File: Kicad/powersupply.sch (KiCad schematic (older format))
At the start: 43 parts, among them J901 Jack-DC, J902 Double-mini-DIN-6, J903 Conn_01x05, J904 Header, J905 Header, J906 Conn_01x06, Q901 BC548, SW901 SW_DIP_x01, SW902 SW_DIP_x01, U901 5V DC-DC Module, U902 MAX1615, U903 STM32F031K6T6, U904 TLV1117 3.3V 1A

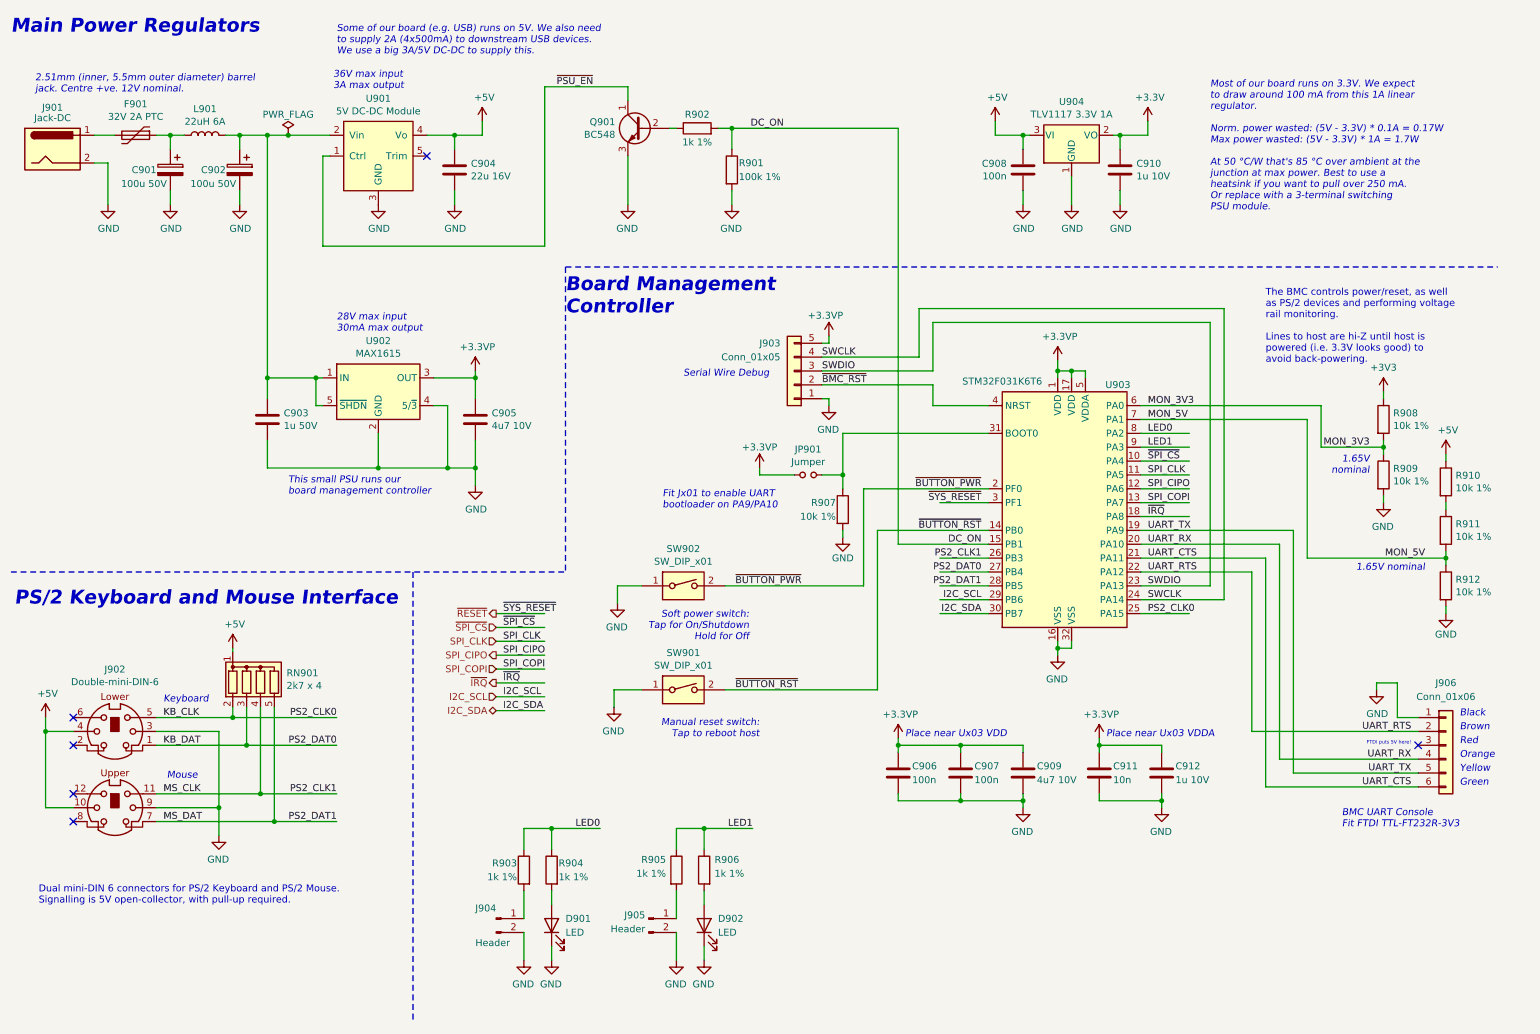
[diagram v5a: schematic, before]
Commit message: Changes to BMC
* Swapped BUTTON_PWR and SYS_RESET to avoid DRC issue
* Split PSU and BMC into two separate sheets
* Swapped some pins on the STM32 to make it compatible with more
alternatives
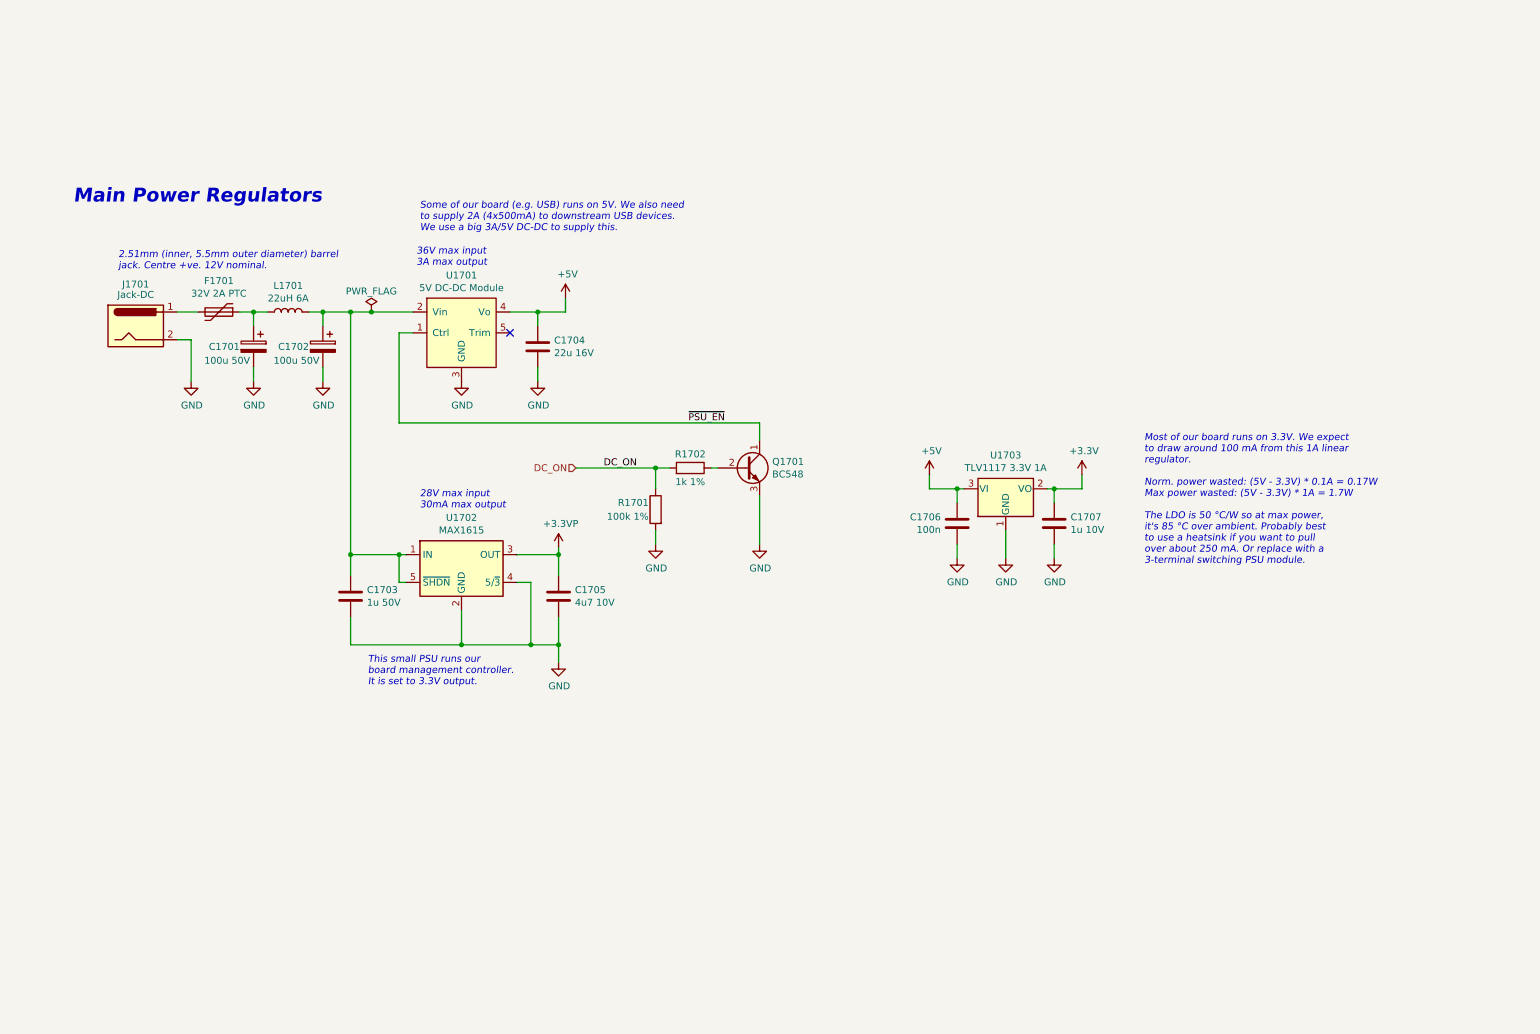
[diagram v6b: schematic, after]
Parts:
- removed C904: 22u 16V, Capacitor_SMD:C_0805_2012Metric_Pad1.18x1.45mm_HandSolder, symbol Device:C
- removed C906, C907, C908: 100n, Capacitor_SMD:C_0805_2012Metric_Pad1.18x1.45mm_HandSolder, symbol Device:C
- removed C909: 4u7 10V, Capacitor_SMD:C_0805_2012Metric_Pad1.18x1.45mm_HandSolder, symbol Device:C
- removed C910, C912: 1u 10V, Capacitor_SMD:C_0805_2012Metric_Pad1.18x1.45mm_HandSolder, symbol Device:C
- removed C911: 10n, Capacitor_SMD:C_0805_2012Metric_Pad1.18x1.45mm_HandSolder, symbol Device:C
- removed D901, D902: LED, LED_THT:LED_D3.0mm, symbol Device:LED
- removed F901: 32V 2A PTC, Fuse:Fuse_BelFuse_0ZRE0016FF_L9.9mm_W3.8mm, symbol Device:Polyfuse
- removed J901: Jack-DC, Connector_BarrelJack:BarrelJack_CUI_PJ-063AH_Horizontal, symbol Connector:Jack-DC
- removed J902: Double-mini-DIN-6, Neotron-Common-Hardware:Double_mini-DIN_6, symbol Neotron-Common-Hardware:Double-mini-DIN-6
- removed J903: Conn_01x05, Connector_PinHeader_2.54mm:PinHeader_1x05_P2.54mm_Vertical, symbol Connector_Generic:Conn_01x05
- removed J904, J905: Header, Connector_PinHeader_2.54mm:PinHeader_1x02_P2.54mm_Vertical, symbol Connector:Conn_01x02_Male
- removed J906: Conn_01x06, Connector_PinHeader_2.54mm:PinHeader_1x06_P2.54mm_Vertical, symbol Connector_Generic:Conn_01x06
- removed JP901: Jumper, Connector_PinHeader_2.54mm:PinHeader_1x02_P2.54mm_Vertical, symbol Device:Jumper_NO_Small
- removed L901: 22uH 6A, Inductor_THT:L_Axial_L26.7mm_D12.1mm_P35.00mm_Horizontal_Vishay_IHA-103, symbol Device:L
- removed R901: 100k 1%, Resistor_SMD:R_0805_2012Metric_Pad1.20x1.40mm_HandSolder, symbol Device:R
- removed R903, R904, R905, R906: 1k 1%, Resistor_SMD:R_0805_2012Metric_Pad1.20x1.40mm_HandSolder, symbol Device:R
- removed R907, R908, R909, R910, R911, R912: 10k 1%, Resistor_SMD:R_0805_2012Metric_Pad1.20x1.40mm_HandSolder, symbol Device:R
- removed RN901: 2k7 x 4, Resistor_THT:R_Array_SIP5, symbol Device:R_Network04
- removed SW901, SW902: SW_DIP_x01, Connector_PinHeader_2.54mm:PinHeader_1x02_P2.54mm_Vertical, symbol Switch:SW_DIP_x01
- removed U901: 5V DC-DC Module, Neotron-Common-Hardware:K78xx-3AR3, symbol Neotron-Common-Hardware:K78(L)05-3AR3
- removed U902: MAX1615, Package_TO_SOT_SMD:SOT-23-5, symbol Regulator_Linear:MAX1615xUK
- removed U903: STM32F031K6T6, Package_QFP:LQFP-32_7x7mm_P0.8mm, symbol MCU_ST_STM32F0:STM32F031K6Tx
- added C1704: 22u 16V, Capacitor_SMD:C_0805_2012Metric_Pad1.18x1.45mm_HandSolder, symbol Device:C
- added C1706: 100n, Capacitor_SMD:C_0805_2012Metric_Pad1.18x1.45mm_HandSolder, symbol Device:C
- added C1707: 1u 10V, Capacitor_SMD:C_0805_2012Metric_Pad1.18x1.45mm_HandSolder, symbol Device:C
- added F1701: 32V 2A PTC, Fuse:Fuse_BelFuse_0ZRE0016FF_L9.9mm_W3.8mm, symbol Device:Polyfuse
- added J1701: Jack-DC, Connector_BarrelJack:BarrelJack_CUI_PJ-063AH_Horizontal, symbol Connector:Jack-DC
- added L1701: 22uH 6A, Inductor_THT:L_Axial_L26.7mm_D12.1mm_P35.00mm_Horizontal_Vishay_IHA-103, symbol Device:L
- added R1701: 100k 1%, Resistor_SMD:R_0805_2012Metric_Pad1.20x1.40mm_HandSolder, symbol Device:R
- added U1701: 5V DC-DC Module, Neotron-Common-Hardware:K78xx-3AR3, symbol Neotron-Common-Hardware:K78(L)05-3AR3
- added U1702: MAX1615, Package_TO_SOT_SMD:SOT-23-5, symbol Regulator_Linear:MAX1615xUK
- renumbered C901 to C1701, C902 to C1702, C903 to C1703, C905 to C1705, Q901 to Q1701, R902 to R1702, U904 to U1703
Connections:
- net labels removed: +3V3, I2C_SCL, I2C_SDA, KB_CLK, KB_DAT, LED0, LED1, MON_3V3, MON_5V, MS_CLK, MS_DAT, PS2_CLK0, PS2_CLK1, PS2_DAT0, PS2_DAT1, SPI_CIPO, SPI_CLK, SPI_COPI, SWCLK, SWDIO, UART_CTS, UART_RTS, UART_RX, UART_TX, ~BMC_RST, ~BUTTON_PWR, ~BUTTON_RST, ~IRQ, ~RESET, ~SPI_CS, ~SYS_RESET
- wire segments 215 -> 57
- no-connect marks 6 -> 1
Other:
- note added: "Most of our board runs on 3.3V. We expect\nto draw around 100 mA from this 1A linear\nregulator.\n\nNorm. power wasted: (5V - 3.3V) * 0.1A = 0.17W\nMax power wasted: (5V - 3.3V) * 1A = 1.7W\n\nThe LDO is 50 °C/W so at max power,\nit's 85 °C over ambient. Probably best\nto use a heatsink if you want to pull\nover about 250 mA. Or replace with a\n3-terminal switching PSU module."
- note added: "This small PSU runs our\nboard management controller.\nIt is set to 3.3V output."
- note removed: "1.65V nominal"
- note removed: "1.65V\nnominal"
- note removed: "BMC UART Console\nFit FTDI TTL-FT232R-3V3"
- note removed: "Black"
- note removed: "Board Management\nController"
- note removed: "Brown"
- note removed: "Dual mini-DIN 6 connectors for PS/2 Keyboard and PS/2 Mouse.\nSignalling is 5V open-collector, with pull-up required."
- note removed: "FTDI puts 5V here!"
- note removed: "Fit Jx01 to enable UART\nbootloader on PA9/PA10"
- note removed: "Green"
- note removed: "Keyboard"
- note removed: "Manual reset switch:\nTap to reboot host"
- note removed: "Most of our board runs on 3.3V. We expect\nto draw around 100 mA from this 1A linear\nregulator.\n\nNorm. power wasted: (5V - 3.3V) * 0.1A = 0.17W\nMax power wasted: (5V - 3.3V) * 1A = 1.7W\n\nAt 50 °C/W that's 85 °C over ambient at the\njunction at max power. Best to use a\nheatsink if you want to pull over 250 mA.\nOr replace with a 3-terminal switching\nPSU module."
- note removed: "Mouse"
- note removed: "Orange"
- note removed: "PS/2 Keyboard and Mouse Interface"
- note removed: "Place near Ux03 VDD"
- note removed: "Place near Ux03 VDDA"
- note removed: "Red"
- note removed: "Serial Wire Debug"
- note removed: "Soft power switch:\nTap for On/Shutdown\nHold for Off"
- note removed: "The BMC controls power/reset, as well\nas PS/2 devices and performing voltage\nrail monitoring.\n\nLines to host are hi-Z until host is\npowered (i.e. 3.3V looks good) to\navoid back-powering."
- note removed: "This small PSU runs our\nboard management controller"
- note removed: "Yellow"
- moved on the sheet: C1701, C1702, C1703, C1705, Q1701, R1702, U1703

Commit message: Revised PSU switch-on circuit.
Updated notes on BMC and Audio sheet.
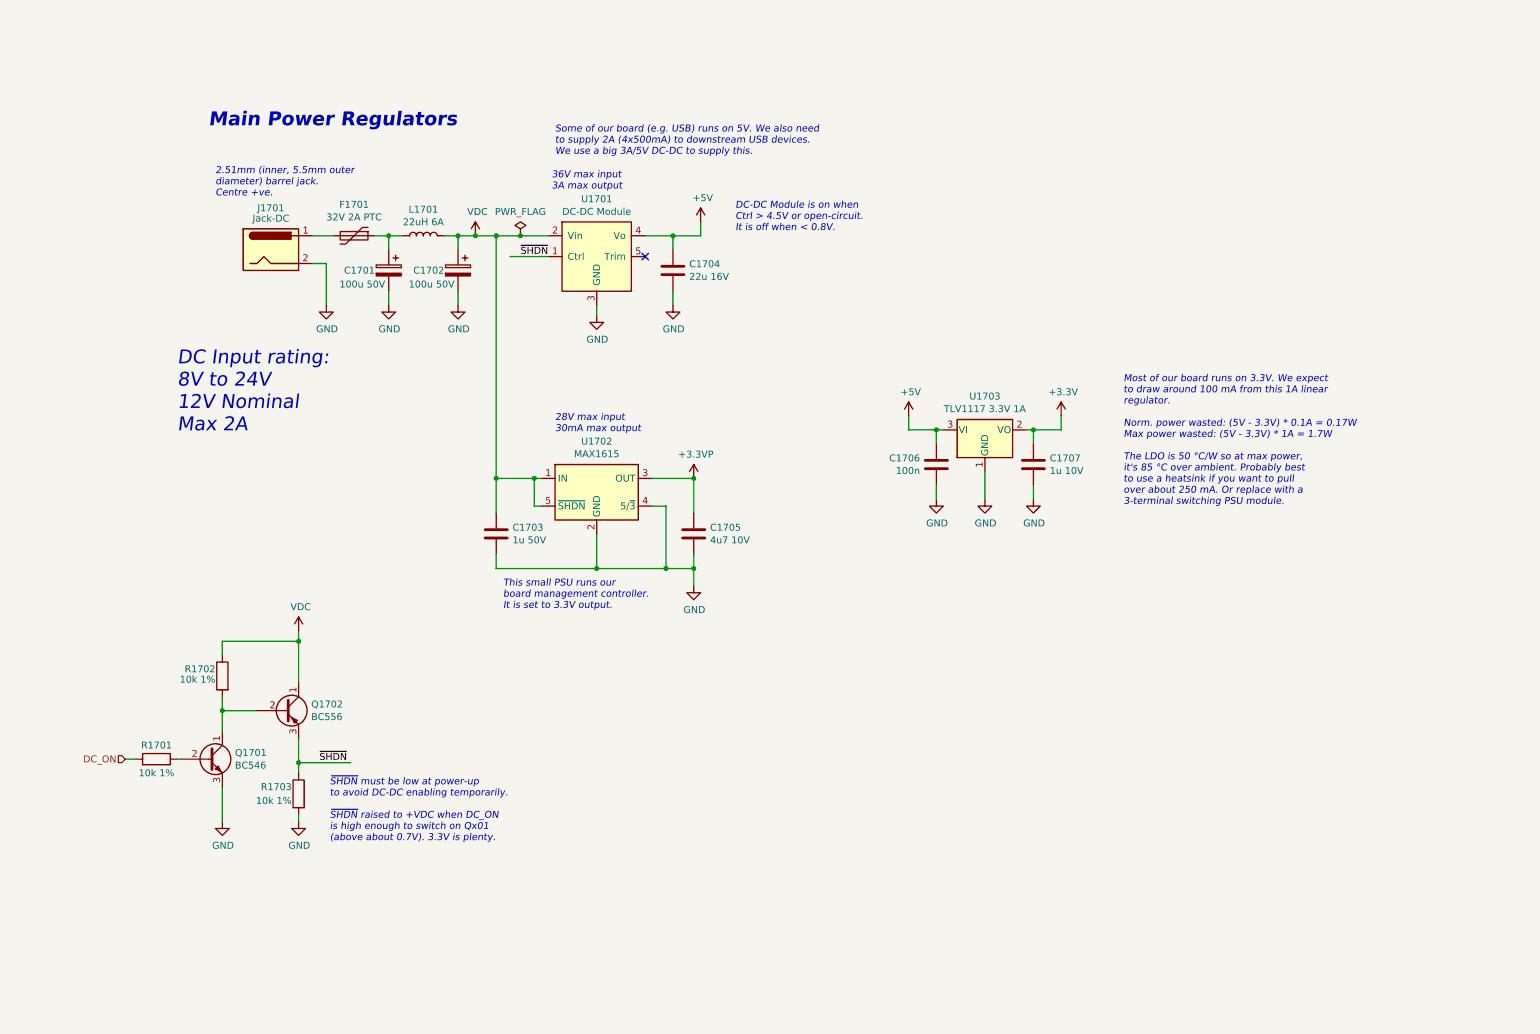
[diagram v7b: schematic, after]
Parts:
- removed Q1701: BC548, Package_TO_SOT_THT:TO-92_HandSolder, symbol Transistor_BJT:BC548
- added Q1701: BC546, Package_TO_SOT_THT:TO-92_Inline, symbol Transistor_BJT:BC546
- added Q1702: BC556, Package_TO_SOT_THT:TO-92_Inline, symbol Transistor_BJT:BC556
- added R1701: 10k 1%, Resistor_SMD:R_0805_2012Metric_Pad1.20x1.40mm_HandSolder, symbol Device:R
- R1702: value 1k 1% -> 10k 1%; Digikey RMCF0805FT1K00-ND -> RMCF0805FT10K0-ND; MPN RMCF0805FT1K00 -> RMCF0805FT10K0
- R1703: renamed from R1701; value 100k 1% -> 10k 1%; Digikey RMCF0805FT100K-ND -> RMCF0805FT10K0-ND; MPN RMCF0805FT100K -> RMCF0805FT10K0
- U1701: value 5V DC-DC Module -> DC-DC Module
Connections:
- net labels added: VDC, ~SHDN
- net labels removed: ~PSU_EN
- wire segments 57 -> 63
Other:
- note added: "2.51mm (inner, 5.5mm outer\ndiameter) barrel jack.\nCentre +ve."
- note added: "DC Input rating:\n8V to 24V\n12V Nominal\nMax 2A"
- note added: "DC-DC Module is on when\nCtrl > 4.5V or open-circuit.\nIt is off when < 0.8V."
- note added: "~SHDN~ must be low at power-up\nto avoid DC-DC enabling temporarily.\n\n~SHDN~ raised to +VDC when DC_ON\nis high enough to switch on Qx01\n(above about 0.7V). 3.3V is plenty."
- note removed: "2.51mm (inner, 5.5mm outer diameter) barrel\njack. Centre +ve. 12V nominal."
- moved on the sheet: C1701, C1702, C1703, C1704, C1705, C1706, C1707, F1701, J1701, L1701, R1703, U1701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
